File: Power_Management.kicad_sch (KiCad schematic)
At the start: 21 parts, among them J1 BATT, Q1 2N7002, U1 BQ24075RGT, U2 MAX17048

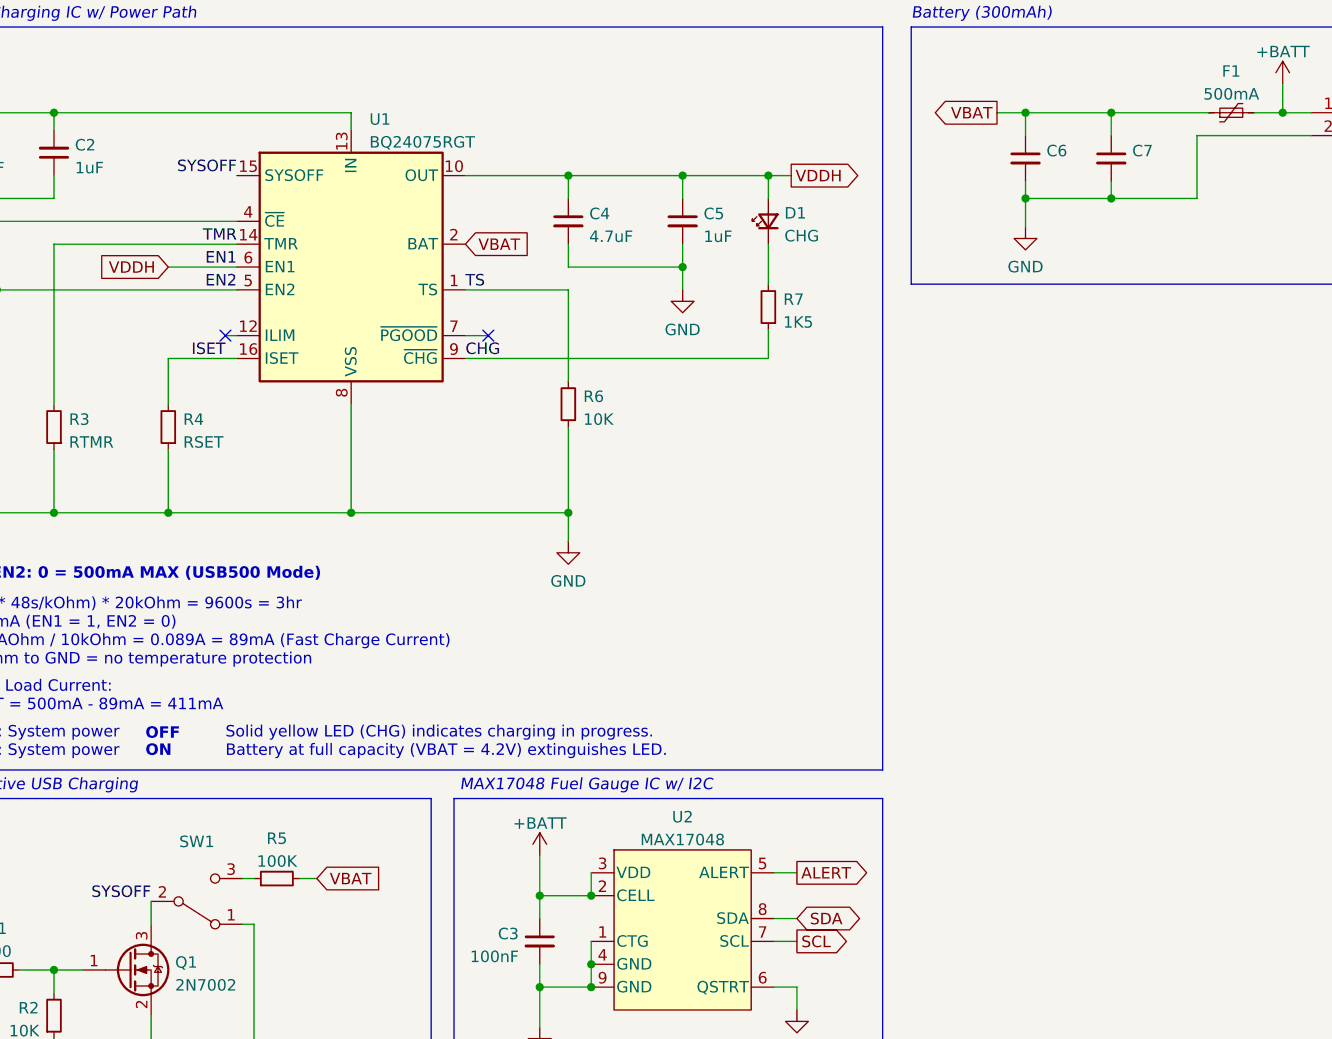
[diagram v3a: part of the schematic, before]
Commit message: fix(schematic): Fix links to footprints
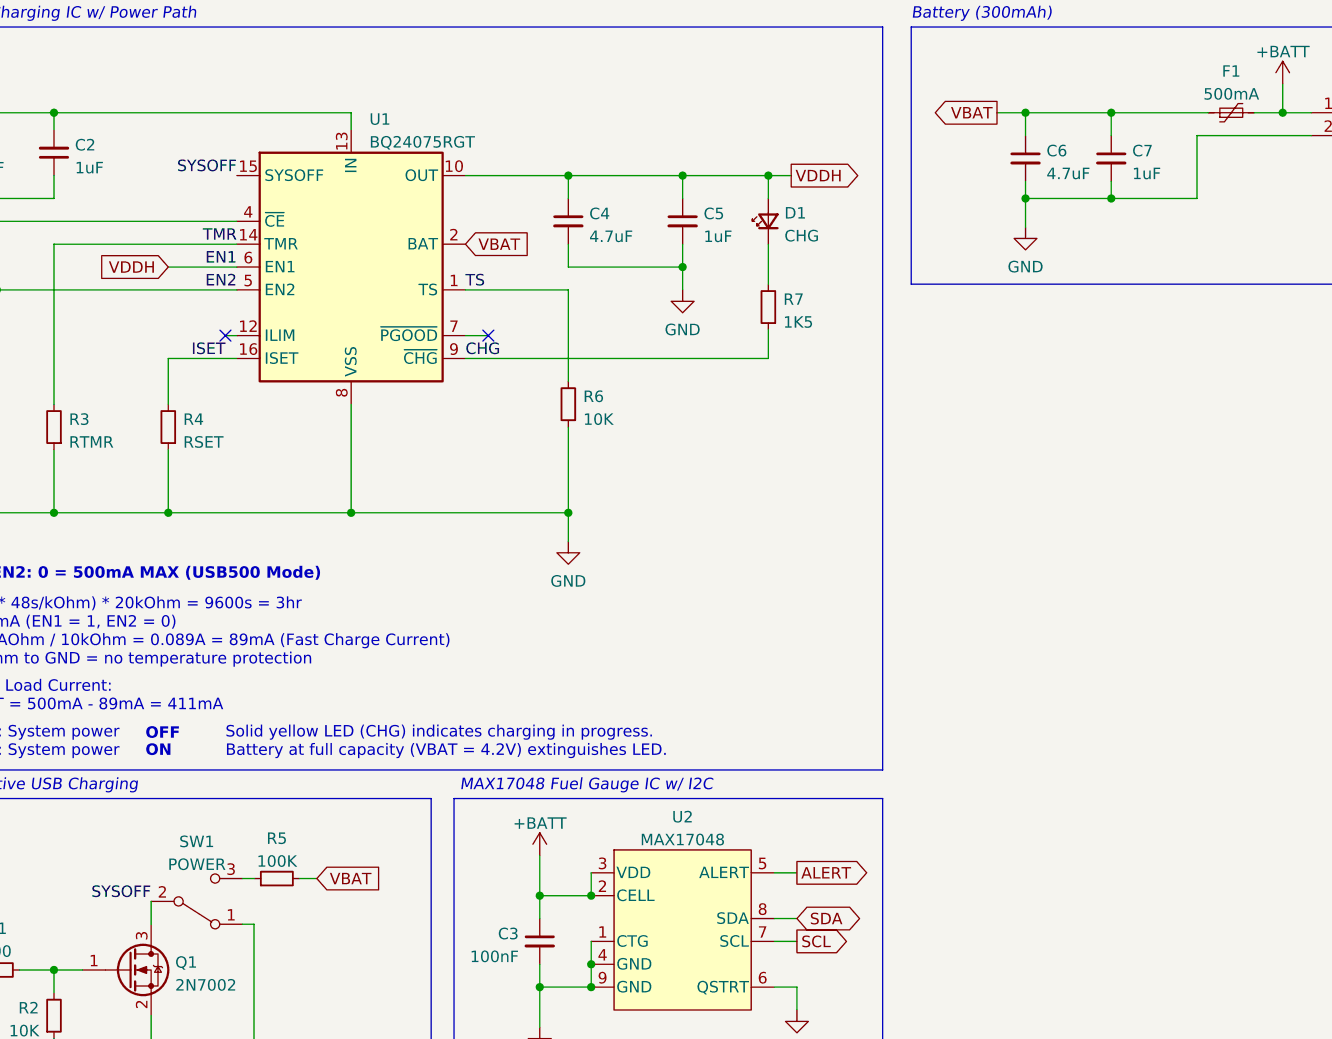
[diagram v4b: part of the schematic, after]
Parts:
- C6: value (none) -> 4.7uF; footprint (none) -> Capacitor_SMD:C_0402_1005Metric
- C7: value (none) -> 1uF; footprint (none) -> Capacitor_SMD:C_0402_1005Metric
- SW1: value (none) -> POWER; footprint (none) -> Athena54:SW_MSK12C02-HB (Reversible)
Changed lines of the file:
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@@
     (in_bom yes) (on_board yes) (fields_autoplaced)
     (property "Reference" "SW1" (id 0) (at 47.625 112.7592 0))
-    (property "Value" "" (id 1) (at 47.625 115.2961 0))
-    (property "Footprint" "" (id 2) (at 47.625 119.38 0)
+    (property "Value" "POWER" (id 1) (at 47.625 115.2961 0))
+    (property "Footprint" "Athena54:SW_MSK12C02-HB (Reversible)" (id 2) (at 47.625 119.38 0)
       (effects (font (size 1.27 1.27)) hide)
     )
@@
       (effects (font (size 1.27 1.27)) (justify left))
     )
-    (property "Value" "" (id 1) (at 142.0241 38.5385 0)
-      (effects (font (size 1.27 1.27)) (justify left))
-    )
-    (property "Footprint" "" (id 2) (at 139.7 36.83 0)
+    (property "Value" "4.7uF" (id 1) (at 142.0241 38.5385 0)
+      (effects (font (size 1.27 1.27)) (justify left))
+    )
+    (property "Footprint" "Capacitor_SMD:C_0402_1005Metric" (id 2) (at 139.7 36.83 0)
       (effects (font (size 1.27 1.27)) hide)
     )
@@
       (effects (font (size 1.27 1.27)) (justify left))
     )
-    (property "Value" "" (id 1) (at 151.5491 38.5385 0)
-      (effects (font (size 1.27 1.27)) (justify left))
-    )
-    (property "Footprint" "" (id 2) (at 149.225 36.83 0)
-      (effects (font (size 1.27 1.27)) hide)
-    )
+    (property "Value" "1uF" (id 1) (at 151.5491 38.5385 0)
+      (effects (font (size 1.27 1.27)) (justify left))
+    )
+    (property "Footprint" "Capacitor_SMD:C_0402_1005Metric" (id 2) (at 149.225 36.83 0)
+      (effects (font (size 1.27 1.27)) hide)
+    )

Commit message: refactor!!!(repository): Rename from Athena54 to Conejo
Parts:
- D1: footprint Athena54:LED_1206_3216Metric (Reversible) -> Conejo:LED_1206_3216Metric (Reversible)
- J1: footprint Athena54:Battery Header -> Conejo:Battery Header
- SW1: footprint Athena54:SW_MSK12C02-HB (Reversible) -> Conejo:SW_MSK12C02-HB (Reversible)
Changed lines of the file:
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@@
     (property "Reference" "SW1" (id 0) (at 47.625 112.7592 0))
     (property "Value" "POWER" (id 1) (at 47.625 115.2961 0))
-    (property "Footprint" "Athena54:SW_MSK12C02-HB (Reversible)" (id 2) (at 47.625 119.38 0)
+    (property "Footprint" "Conejo:SW_MSK12C02-HB (Reversible)" (id 2) (at 47.625 119.38 0)
       (effects (font (size 1.27 1.27)) hide)
     )
@@
       (effects (font (size 1.27 1.27)) (justify right))
     )
-    (property "Footprint" "Athena54:LED_1206_3216Metric (Reversible)" (id 2) (at 111.125 43.815 90)
+    (property "Footprint" "Conejo:LED_1206_3216Metric (Reversible)" (id 2) (at 111.125 43.815 90)
       (effects (font (size 1.27 1.27)) hide)
     )
@@
       (effects (font (size 1.27 1.27)) (justify left))
     )
-    (property "Footprint" "Athena54:Battery Header" (id 2) (at 176.53 31.75 0)
-      (effects (font (size 1.27 1.27)) hide)
-    )
+    (property "Footprint" "Conejo:Battery Header" (id 2) (at 176.53 31.75 0)
+      (effects (font (size 1.27 1.27)) hide)
+    )

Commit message: fix(schematic): Further updates to referencing footprints and symbols
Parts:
- U2: symbol Thanatos52:MAX17048 -> Conejo:MAX17048
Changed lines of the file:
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@@
       (effects (font (size 1.27 1.27) italic) (justify left) hide)
     )
-    (property "Datasheet" "" (id 3) (at 40.005 127 0)
+    (property "Datasheet" "http://www.aosmd.com/pdfs/datasheet/AO3400A.pdf" (id 3) (at 40.005 127 0)
       (effects (font (size 1.27 1.27)) (justify left) hide)
     )
@@
     (pin "2")
   )
-  (symbol (lib_id "Thanatos52:MAX17048") (at 101.6 122.555 0) (unit 1)
+  (symbol (lib_id "Conejo:MAX17048") (at 101.6 122.555 0) (unit 1)
     (in_bom yes) (on_board yes) (fields_autoplaced)
     (property "Reference" "U2" (id 0) (at 101.6 110.016 0))

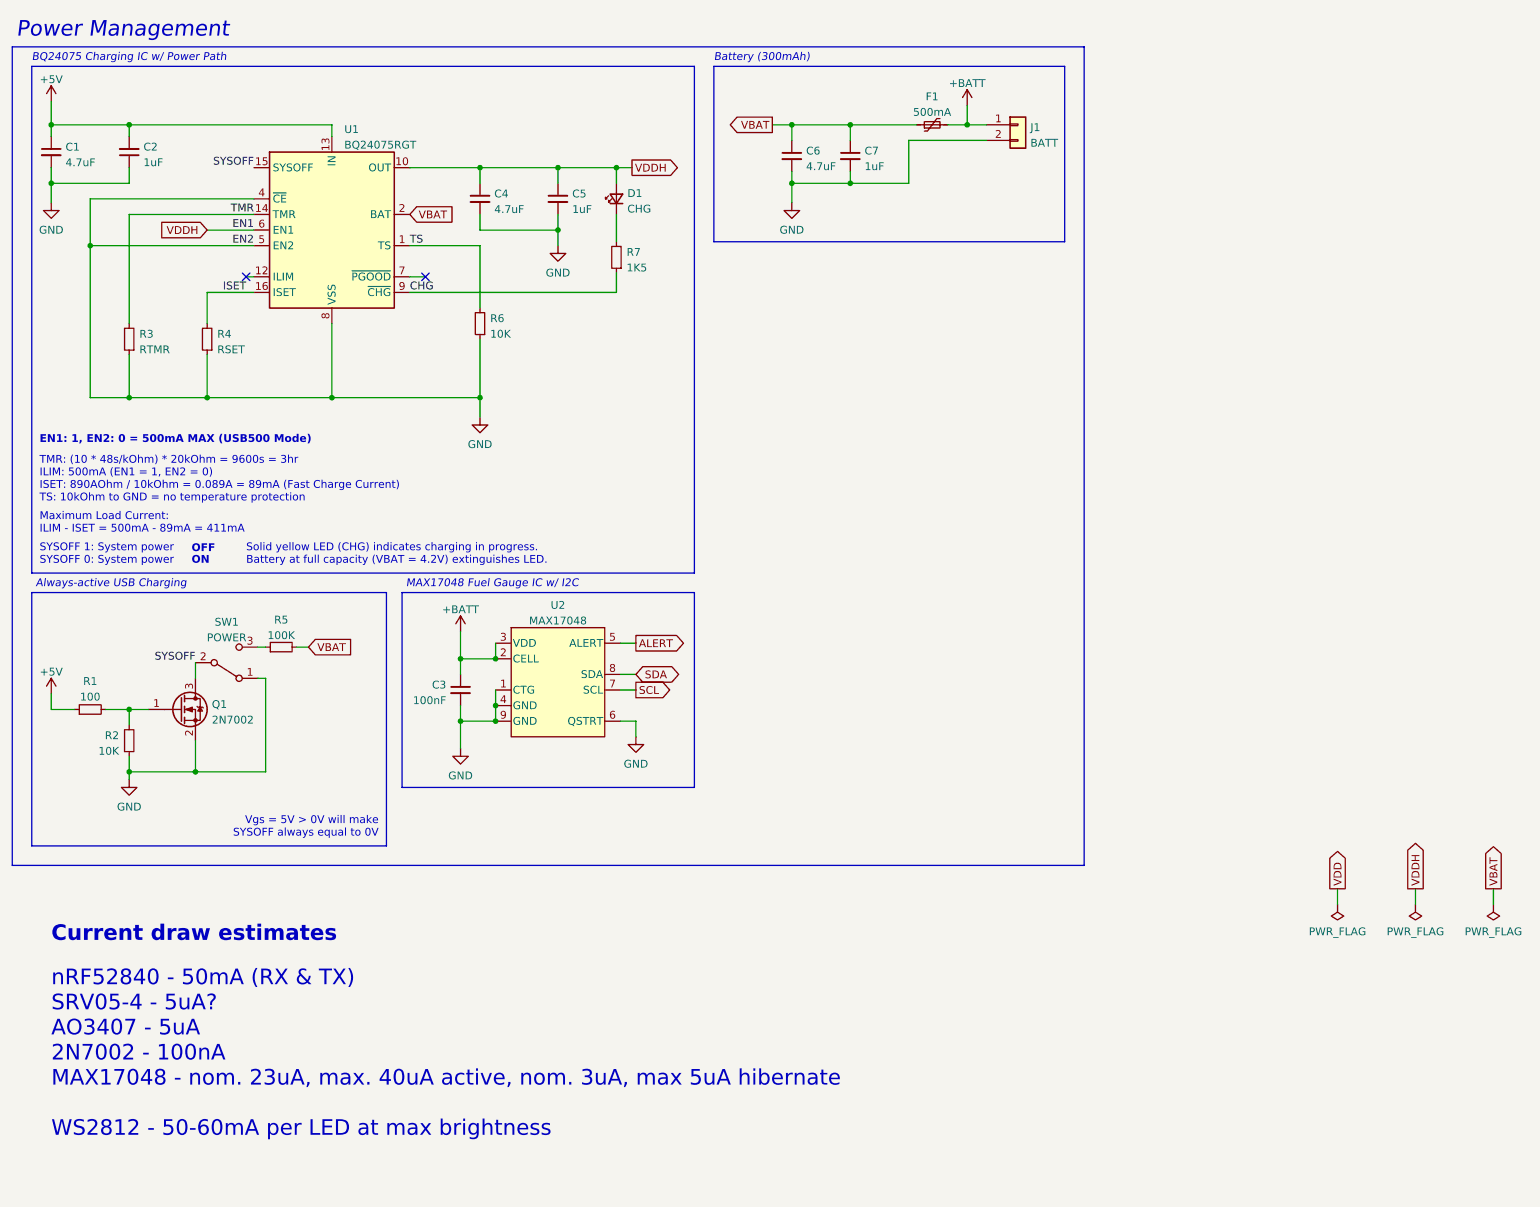
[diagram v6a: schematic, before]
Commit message: feat(pcb): Version 0.2.2
- Update MS88SF3 footprint
- Create thumb cluster silksscreen
- Separate NTPH and PTH drill files
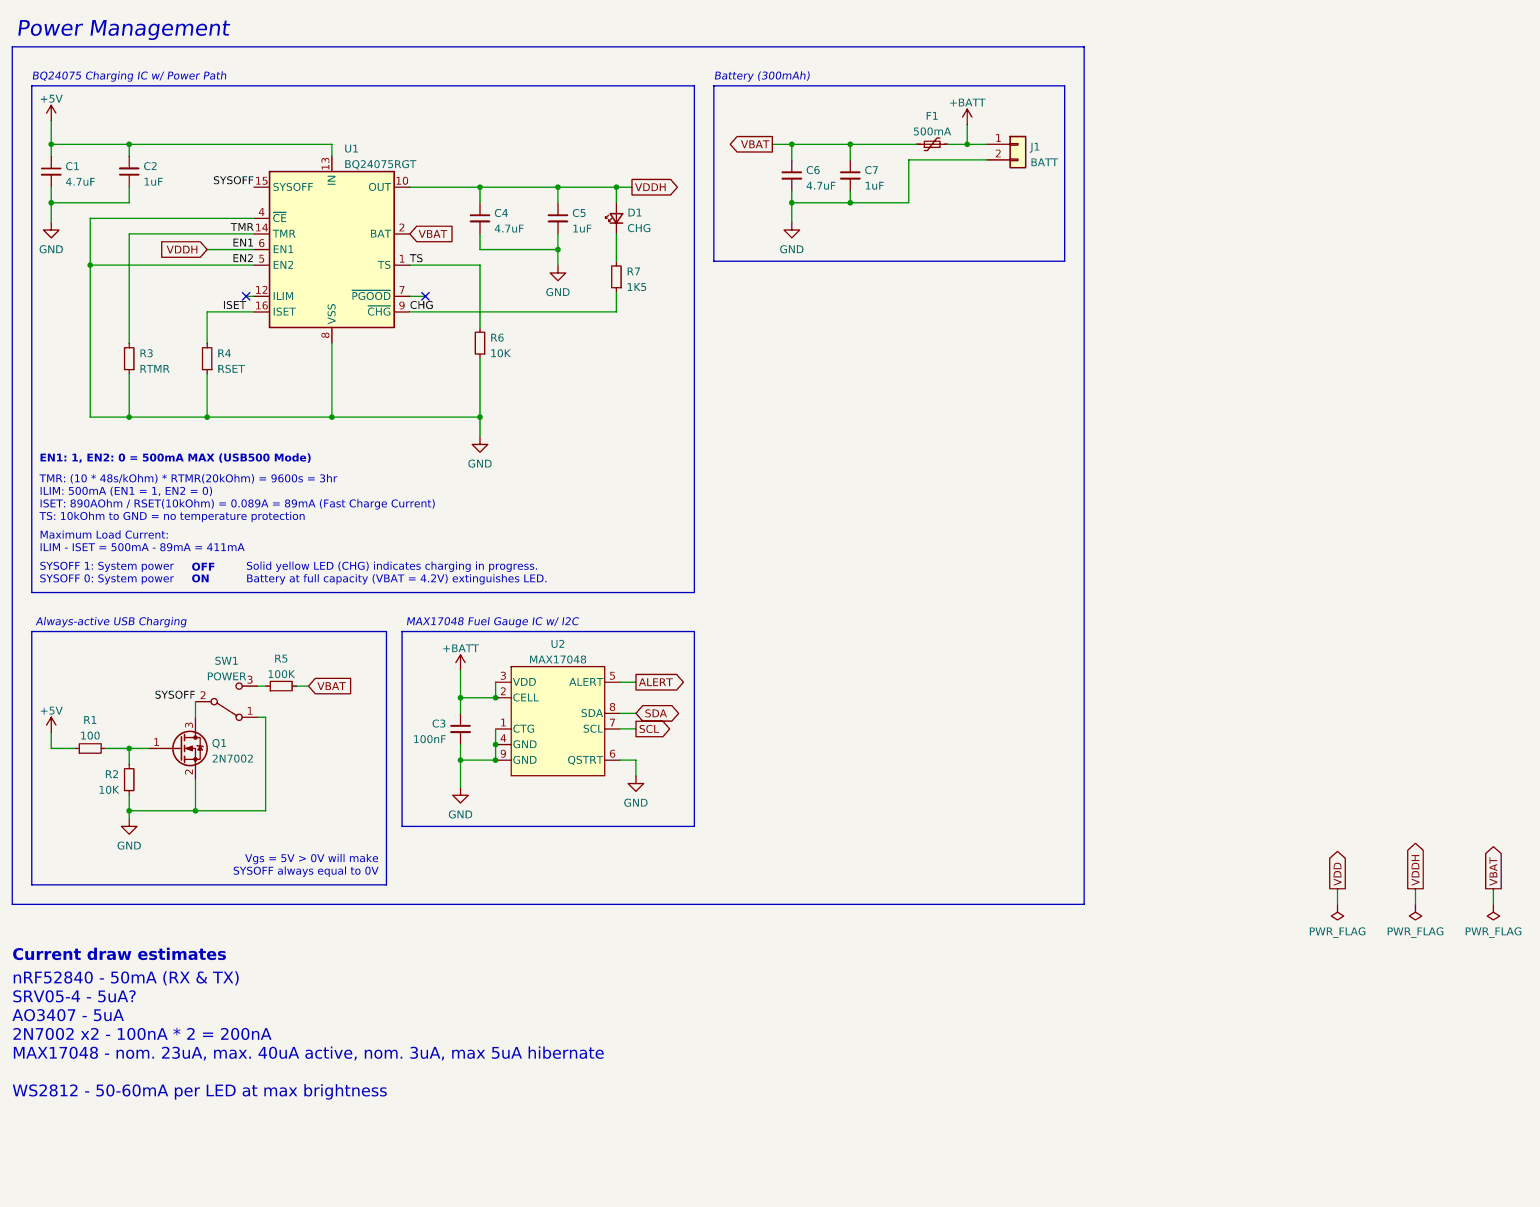
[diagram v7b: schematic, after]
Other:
- note added: "TMR: (10 * 48s/kOhm) * RTMR(20kOhm) = 9600s = 3hr ILIM: 500mA (EN1 = 1, EN2 = 0) ISET: 890AOhm / RSET(10kOhm) = 0.089A = 89mA (Fast Charge Current) TS: 10kOhm to GND = no temperature protection"
- note added: "nRF52840 - 50mA (RX & TX) SRV05-4 - 5uA? AO3407 - 5uA 2N7002 x2 - 100nA * 2 = 200nA MAX17048 - nom. 23uA, max. 40uA active, nom. 3uA, max 5uA hibernate WS2812 - 50-60mA per LED at max brightness"
- note removed: "TMR: (10 * 48s/kOhm) * 20kOhm = 9600s = 3hr ILIM: 500mA (EN1 = 1, EN2 = 0) ISET: 890AOhm / 10kOhm = 0.089A = 89mA (Fast Charge Current) TS: 10kOhm to GND = no temperature protection"
- note removed: "nRF52840 - 50mA (RX & TX) SRV05-4 - 5uA? AO3407 - 5uA 2N7002 - 100nA MAX17048 - nom. 23uA, max. 40uA active, nom. 3uA, max 5uA hibernate WS2812 - 50-60mA per LED at max brightness"
- moved on the sheet: C1, C2, C3, C4, C5, C6, C7, D1, F1, J1, Q1, R1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

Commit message: feat(pcb): Version 0.3
- Move components entirely to back copper :tada:
- Update silkscreen legibility to enhance ease of component placement
- Fix I2C pullup resistors
  - Replace incorrect value of 1K5 with 5K1
  - Update footprint to 0603_1608 to fit VDD traces underneath, compared to original 0402_1005 footprint
- Increase text width on RESET button, POWER Switch, and CHG LED
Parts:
- C1, C4, C6: value 4.7uF -> 4u7F
- renumbered C5 to C3, C3 to C5, R3 to R1, R4 to R2, R6 to R3, R1 to R4, R2 to R5, R5 to R6
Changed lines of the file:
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@@
       (effects (font (size 1.27 1.27)) (justify left))
     )
-    (property "Value" "4.7uF" (id 1) (at 142.0241 41.7135 0)
+    (property "Value" "4u7F" (id 1) (at 142.0241 41.7135 0)
       (effects (font (size 1.27 1.27)) (justify left))
     )
@@
   (symbol (lib_id "Device:R_Small") (at 25.4 133.35 90) (unit 1)
     (in_bom yes) (on_board yes) (fields_autoplaced)
-    (property "Reference" "R1" (id 0) (at 25.4 128.7612 90))
+    (property "Reference" "R4" (id 0) (at 25.4 128.7612 90))
     (property "Value" "100" (id 1) (at 25.4 131.2981 90))
     (property "Footprint" "Resistor_SMD:R_0402_1005Metric" (id 2) (at 25.4 133.35 0)
@@
   (symbol (lib_id "Device:R_Small") (at 31.75 69.85 180) (unit 1)
     (in_bom yes) (on_board yes)
-    (property "Reference" "R3" (id 0) (at 33.401 69.0153 0)
+    (property "Reference" "R1" (id 0) (at 33.401 69.0153 0)
       (effects (font (size 1.27 1.27)) (justify right))
     )
@@
   (symbol (lib_id "Device:R_Small") (at 88.9 67.31 180) (unit 1)
     (in_bom yes) (on_board yes)
-    (property "Reference" "R6" (id 0) (at 90.551 66.4753 0)
+    (property "Reference" "R3" (id 0) (at 90.551 66.4753 0)
       (effects (font (size 1.27 1.27)) (justify right))
     )
@@
   (symbol (lib_id "Device:C_Small") (at 101.6 46.99 0) (unit 1)
     (in_bom yes) (on_board yes) (fields_autoplaced)
-    (property "Reference" "C5" (id 0) (at 103.9241 46.1616 0)
+    (property "Reference" "C3" (id 0) (at 103.9241 46.1616 0)
       (effects (font (size 1.27 1.27)) (justify left))
     )
@@
   (symbol (lib_id "Device:R_Small") (at 56.515 123.19 90) (unit 1)
     (in_bom yes) (on_board yes) (fields_autoplaced)
-    (property "Reference" "R5" (id 0) (at 56.515 118.7536 90))
+    (property "Reference" "R6" (id 0) (at 56.515 118.7536 90))
     (property "Value" "100K" (id 1) (at 56.515 121.2905 90))
     (property "Footprint" "Resistor_SMD:R_0402_1005Metric" (id 2) (at 56.515 123.19 0)
@@
       (effects (font (size 1.27 1.27)) (justify left))
     )
-    (property "Value" "4.7uF" (id 1) (at 21.3741 41.0785 0)
+    (property "Value" "4u7F" (id 1) (at 21.3741 41.0785 0)
       (effects (font (size 1.27 1.27)) (justify left))
     )
@@
       (effects (font (size 1.27 1.27)) (justify left))
     )
-    (property "Value" "4.7uF" (id 1) (at 91.2241 48.6985 0)
+    (property "Value" "4u7F" (id 1) (at 91.2241 48.6985 0)
       (effects (font (size 1.27 1.27)) (justify left))
     )
@@
   (symbol (lib_id "Device:C_Small") (at 85.725 130.175 0) (mirror y) (unit 1)
     (in_bom yes) (on_board yes) (fields_autoplaced)
-    (property "Reference" "C3" (id 0) (at 83.4009 129.3466 0)
+    (property "Reference" "C5" (id 0) (at 83.4009 129.3466 0)
       (effects (font (size 1.27 1.27)) (justify left))
     )
@@
   (symbol (lib_id "Device:R_Small") (at 44.45 69.85 180) (unit 1)
     (in_bom yes) (on_board yes)
-    (property "Reference" "R4" (id 0) (at 46.101 69.0153 0)
+    (property "Reference" "R2" (id 0) (at 46.101 69.0153 0)
       (effects (font (size 1.27 1.27)) (justify right))
     )
@@
   (symbol (lib_id "Device:R_Small") (at 31.75 138.43 0) (mirror x) (unit 1)
     (in_bom yes) (on_board yes)
-    (property "Reference" "R2" (id 0) (at 30.099 137.5953 0)
-      (effects (font (size 1.27 1.27)) (justify right))
-    )
+    (property "Reference" "R5" (id 0) (at 30.099 137.5953 0)
+      (effects (font (size 1.27 1.27)) (justify right))
+    )
